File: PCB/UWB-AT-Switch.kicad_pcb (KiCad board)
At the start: 2 copper layers, 21 x 34 mm, 11 parts, among them J1 S2B-PH-K-SLFSN, J2 Conn_01x02_Pin, J3 Conn_01x02_Pin, J4 Conn_01x02_Pin, U1 J102K1CS33VDC.20

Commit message: silkscreen updated
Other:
- board text added: "UWB-AT - Rev A"
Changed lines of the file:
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@@
   (gr_line (start 150.5 118) (end 149 118)
     (stroke (width 0.1) (type default)) (layer "User.1"))
+  (gr_text "UWB-AT - Rev A" (at 134.5 119.5) (layer "B.SilkS")
+    (effects (font (size 1 1) (thickness 0.15)) (justify right bottom mirror))
+  )
   (gr_text "Color" (at 93.62143 160.75) (layer "Dwgs.User")
     (effects (font (size 1.5 1.5) (thickness 0.3)) (justify left top))

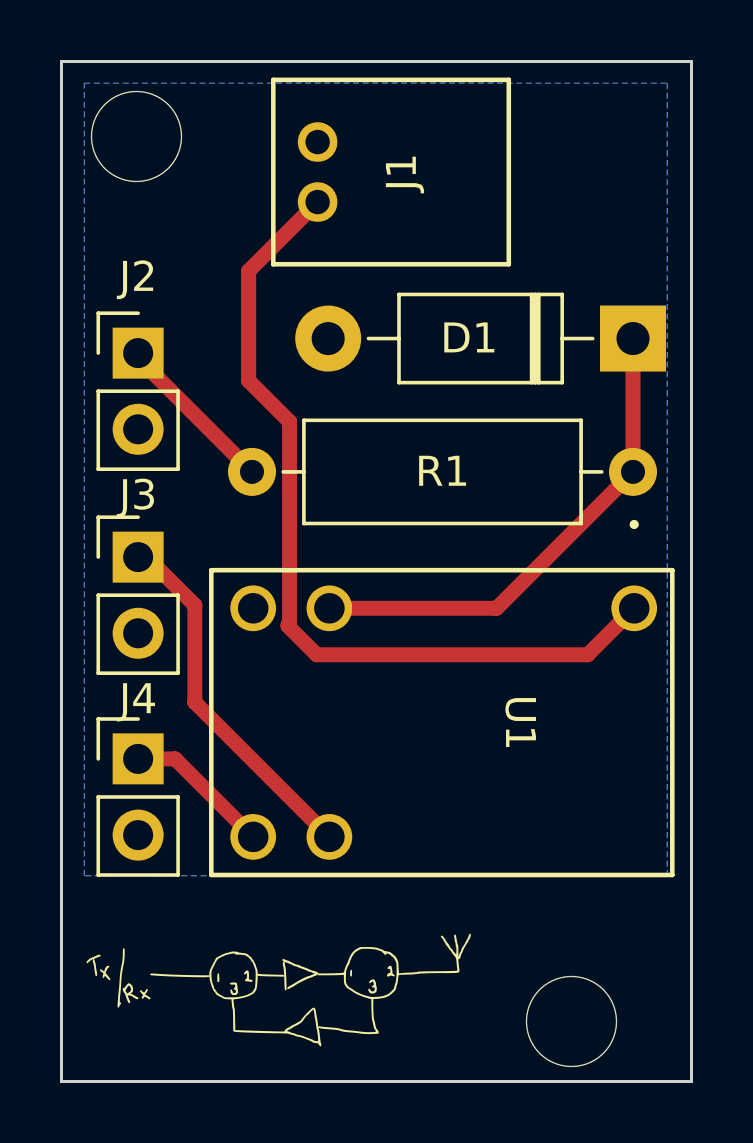
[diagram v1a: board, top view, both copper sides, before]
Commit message: added 3rd mounting hole
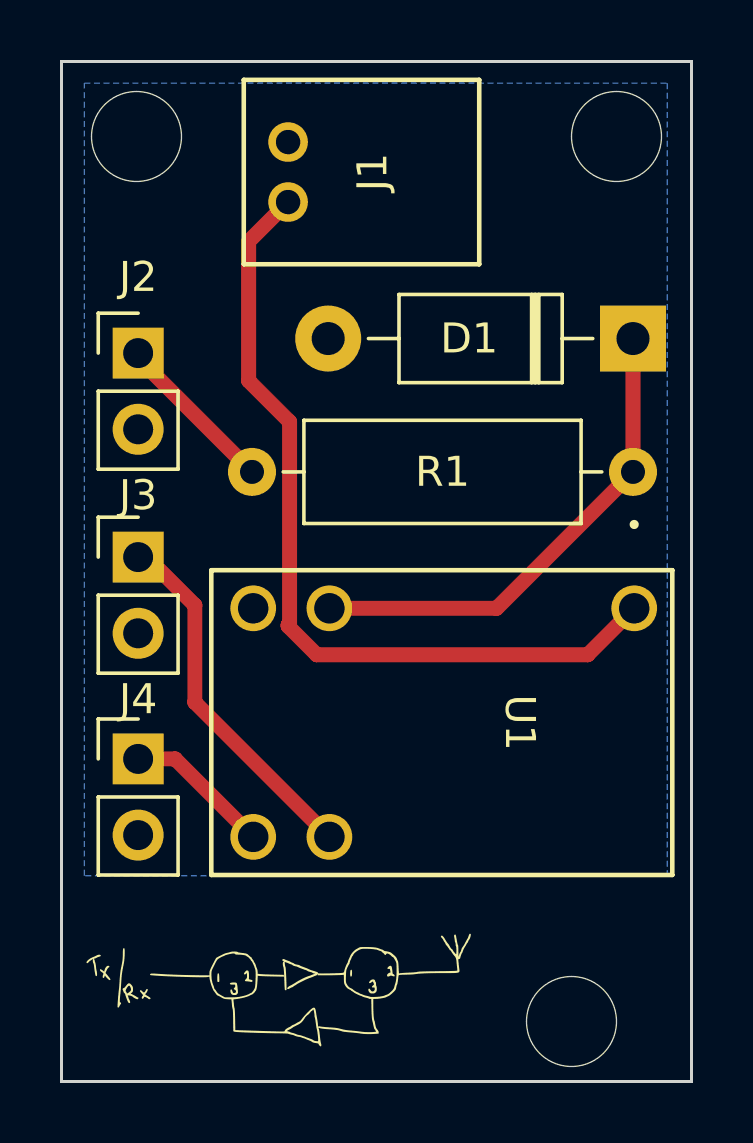
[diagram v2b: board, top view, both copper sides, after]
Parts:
- added REF**: M3, MountingHole:MountingHole_3mm, F.Cu at (152.5, 88.5)
- moved J1 0.98 mm to (141.6, 90.7)
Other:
- board text added: "3 x Ø3.00"
- board text removed: "2 x Ø3.00"
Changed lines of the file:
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@@
   )
   (footprint "footprints:CONN_S2B-PH-K-S_JST" (layer "F.Cu")
-    (at 142.5376 90.6851 90)
+    (at 141.5527 90.6851 90)
     (tags "S2B-PH-K-SLFSN ")
     (property "Sheetfile" "Charging-Switch.kicad_sch")
@@
       (rotate (xyz 0 0 0))
     )
+  )
+  (footprint "MountingHole:MountingHole_3mm" (layer "F.Cu")
+    (at 152.5 88.5)
+    (descr "Mounting Hole 3mm, no annular")
+    (tags "mounting hole 3mm no annular")
+    (attr exclude_from_pos_files exclude_from_bom)
+    (fp_text reference "REF**" (at 0 -4) (layer "F.SilkS") hide
+        (effects (font (size 1 1) (thickness 0.15)))
+    )
+    (fp_text value "M3" (at 0 0) (layer "F.Fab")
+        (effects (font (size 1 1) (thickness 0.15)))
+    )
+    (fp_circle (center 0 0) (end 3 0)
+      (stroke (width 0.15) (type solid)) (fill none) (layer "Cmts.User"))
+    (fp_circle (center 0 0) (end 3.25 0)
+      (stroke (width 0.05) (type solid)) (fill none) (layer "F.CrtYd"))
+    (pad "" np_thru_hole circle (at 0 0) (size 3 3) (drill 3) (layers "F&B.Cu" "*.Mask"))
   )
   (footprint "Diode_THT:D_DO-41_SOD81_P10.16mm_Horizontal" (layer "F.Cu")
@@
   (gr_line (start 155 86) (end 155 120)
     (stroke (width 0.1) (type default)) (layer "Edge.Cuts"))
-  (gr_line (start 136.5 88) (end 136.5 86.5)
+  (gr_line (start 152.5 86.5) (end 152.5 87)
+    (stroke (width 0.1) (type default)) (layer "F.Fab"))
+  (gr_line (start 154 88.5) (end 154.5 88.5)
+    (stroke (width 0.1) (type default)) (layer "F.Fab"))
+  (gr_circle (center 151 118) (end 152.5 118)
+    (stroke (width 0.1) (type default)) (fill none) (layer "F.Fab"))
+  (gr_circle (center 136.5 88.5) (end 138 88.5)
+    (stroke (width 0.1) (type default)) (fill none) (layer "F.Fab"))
+  (gr_line (start 151 88.5) (end 150.5 88.5)
+    (stroke (width 0.1) (type default)) (layer "F.Fab"))
+  (gr_line (start 152.5 90) (end 152.5 90.5)
+    (stroke (width 0.1) (type default)) (layer "F.Fab"))
+  (gr_circle (center 152.5 88.5) (end 153.7 87.6)
+    (stroke (width 0.1) (type default)) (fill none) (layer "F.Fab"))
+  (gr_line (start 136.5 87) (end 136.5 86.5)
     (stroke (width 0.1) (type default)) (layer "User.1"))
   (gr_line (start 151 118.25) (end 151 117.75)
     (stroke (width 0.1) (type default)) (layer "User.1"))
-  (gr_line (start 137 88.5) (end 138.5 88.5)
+  (gr_line (start 138 88.5) (end 138.5 88.5)
     (stroke (width 0.1) (type default)) (layer "User.1"))
   (gr_line (start 151.5 118) (end 153 118)
@@
   (gr_line (start 150.75 118) (end 151.25 118)
     (stroke (width 0.1) (type default)) (layer "User.1"))
-  (gr_circle (center 151 118) (end 152.5 118)
-    (stroke (width 0.15) (type default)) (fill none) (layer "User.1"))
-  (gr_circle (center 136.5 88.5) (end 138 88.5)
-    (stroke (width 0.1) (type default)) (fill none) (layer "User.1"))
-  (gr_line (start 136 88.5) (end 134.5 88.5)
+  (gr_line (start 135 88.5) (end 134.5 88.5)
     (stroke (width 0.1) (type default)) (layer "User.1"))
   (gr_line (start 136.25 88.5) (end 136.75 88.5)
     (stroke (width 0.1) (type default)) (layer "User.1"))
-  (gr_line (start 136.5 89) (end 136.5 90.5)
+  (gr_line (start 136.5 90) (end 136.5 90.5)
     (stroke (width 0.1) (type default)) (layer "User.1"))
   (gr_line (start 151 117.5) (end 151 116)
@@
     (effects (font (size 1.5 1.5) (thickness 0.1)) (justify left top))
   )
-  (gr_text "2 x Ø3.00" (at 139.75 124.5) (layer "Dwgs.User")
+  (gr_text "3 x Ø3.00" (at 139.75 124.5) (layer "Dwgs.User")
     (effects (font (size 1 1) (thickness 0.15)) (justify right))
   )
@@
     (pts (xy 134 86) (xy 155 86))
     (height -10)
-    (gr_text "21.0000 mm" (at 144.5 74.85) (layer "Dwgs.User")
+    (gr_text "21.00 mm" (at 144.5 74.85) (layer "Dwgs.User")
       (effects (font (size 1 1) (thickness 0.15)))
     )
-    (format (prefix "") (suffix "") (units 3) (units_format 1) (precision 4))
+    (format (prefix "") (suffix "") (units 3) (units_format 1) (precision 2))
     (style (thickness 0.15) (arrow_length 1.27) (text_position_mode 0) (extension_height 0.58642) (extension_offset 0.5) keep_text_aligned)
   )
@@
     (style (thickness 0.15) (arrow_length 0.6) (text_position_mode 2) (extension_height 0.58642) (extension_offset 0.5))
   )
+  (dimension (type aligned) (layer "Dwgs.User")
+    (pts (xy 152.5 86) (xy 155 86))
+    (height -5)
+    (gr_text "2.50" (at 150.5 81) (layer "Dwgs.User")
+      (effects (font (size 1 1) (thickness 0.15)))
+    )
+    (format (prefix "") (suffix "") (units 3) (units_format 0) (precision 2))
+    (style (thickness 0.15) (arrow_length 0.6) (text_position_mode 2) (extension_height 0.58642) (extension_offset 0.5) keep_text_aligned)
+  )
   (segment (start 153.05 95.235) (end 153.05 99.68) (width 0.5) (layer "F.Cu") (net 1))
   (segment (start 148.5034 104.2266) (end 153.05 99.68) (width 0.5) (layer "F.Cu") (net 1))
   (segment (start 142.9301 104.2266) (end 148.5034 104.2266) (width 0.5) (layer "F.Cu") (net 1))
-  (segment (start 141.6021 104.728627) (end 141.6021 100.21) (width 0.5) (layer "F.Cu") (net 3))
-  (segment (start 141.6021 98.0071) (end 141.6021 100.21) (width 0.5) (layer "F.Cu") (net 3))
+  (segment (start 141.6021 104.728627) (end 141.6021 98.0071) (width 0.5) (layer "F.Cu") (net 3))
+  (segment (start 140.2376 92.000201) (end 141.5527 90.685101) (width 0.5) (layer "F.Cu") (net 3))
+  (segment (start 151.5407 105.776) (end 142.509 105.776) (width 0.5) (layer "F.Cu") (net 3))
+  (segment (start 141.6021 98.0071) (end 140.2376 96.6426) (width 0.5) (layer "F.Cu") (net 3))
+  (segment (start 141.555 104.822) (end 141.555 104.775727) (width 0.5) (layer "F.Cu") (net 3))
   (segment (start 153.0901 104.2266) (end 151.5407 105.776) (width 0.5) (layer "F.Cu") (net 3))
-  (segment (start 140.2376 96.6426) (end 141.6021 98.0071) (width 0.5) (layer "F.Cu") (net 3))
-  (segment (start 142.5376 90.685101) (end 140.2376 92.985101) (width 0.5) (layer "F.Cu") (net 3))
+  (segment (start 141.555 104.775727) (end 141.6021 104.728627) (width 0.5) (layer "F.Cu") (net 3))
   (segment (start 142.509 105.776) (end 141.555 104.822) (width 0.5) (layer "F.Cu") (net 3))
-  (segment (start 140.2376 92.985101) (end 140.2376 96.6426) (width 0.5) (layer "F.Cu") (net 3))
-  (segment (start 141.555 104.775727) (end 141.6021 104.728627) (width 0.5) (layer "F.Cu") (net 3))
-  (segment (start 151.5407 105.776) (end 142.509 105.776) (width 0.5) (layer "F.Cu") (net 3))
-  (segment (start 141.555 104.822) (end 141.555 104.775727) (width 0.5) (layer "F.Cu") (net 3))
+  (segment (start 140.2376 96.6426) (end 140.2376 92.000201) (width 0.5) (layer "F.Cu") (net 3))
   (segment (start 136.54 95.87) (end 140.35 99.68) (width 0.5) (layer "F.Cu") (net 4))
   (segment (start 136.54 95.865) (end 136.54 95.87) (width 0.5) (layer "F.Cu") (net 4))

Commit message: changes not saved
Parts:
- removed G***: LOGO, imports:circulator3_silk
- removed G***: LOGO, imports:airtag_silk
